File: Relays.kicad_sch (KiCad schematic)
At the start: 28 parts, among them U6 ULN2003

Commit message: Version 1.1
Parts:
- removed IJ1, IJ2, IJ3, IJ4, NCI1, NCI2, NCI3, NCR1, NCR2, NCR3, RJ1, RJ2, RJ3, RJ4: TestPoint, TestPoint:TestPoint_Pad_D1.0mm, symbol Connector:TestPoint
- renumbered R14 to R17, R13 to R18
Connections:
- net RL2: now also U6.6 (I6)
- net RL3: now also U6.4 (I4)
- net RL4: now also U6.2 (I2)
- net at U6.15 (O2): now also RL1.A2, U6.16 (O1)
- net at U6.13 (O4): now also RL2.A2, U6.14 (O3)
- net at RL3.A2, U6.12 (O5): now also U6.11 (O6)

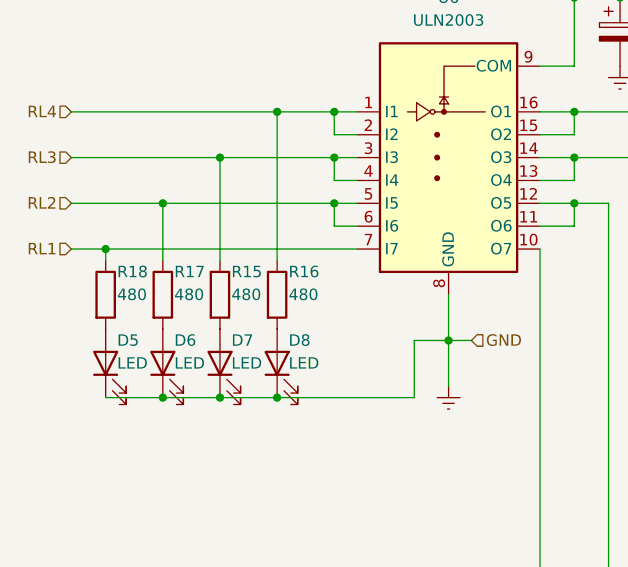
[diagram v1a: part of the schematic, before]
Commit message: Version 1.2 Updates.
Added support for 3 digital switches via ADC.  Added MOV+Fuse protection
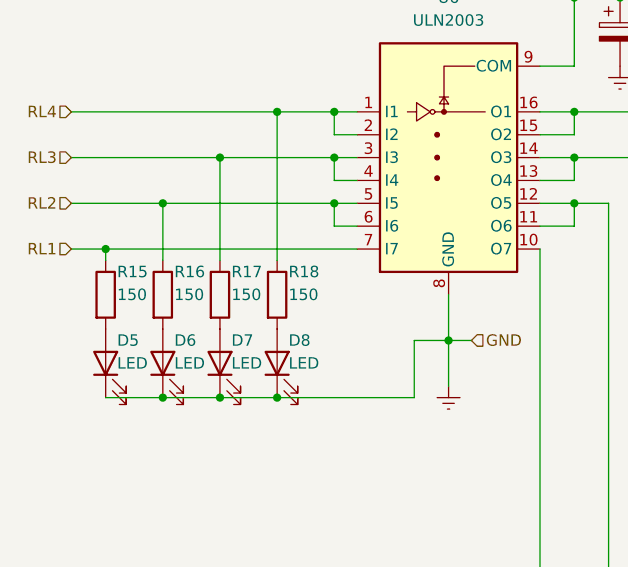
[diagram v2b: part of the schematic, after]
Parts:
- R15: renamed from R18; value 480 -> 150
- R16: renamed from R17; value 480 -> 150
- R17: renamed from R15; value 480 -> 150
- R18: renamed from R16; value 480 -> 150
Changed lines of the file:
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@@
   (symbol (lib_id "Device:R") (at 41.91 107.95 0) (unit 1)
     (in_bom yes) (on_board yes) (dnp no)
-    (property "Reference" "R17" (at 43.18 105.41 0)
-      (effects (font (size 1.27 1.27)) (justify left))
-    )
-    (property "Value" "480" (at 43.18 107.95 0)
+    (property "Reference" "R16" (at 43.18 105.41 0)
+      (effects (font (size 1.27 1.27)) (justify left))
+    )
+    (property "Value" "150" (at 43.18 107.95 0)
       (effects (font (size 1.27 1.27)) (justify left))
     )
@@
       (project "WemosD1Mini-8266"
         (path "/84e8e68d-ec51-4c17-a8b1-603b22d1189f/cc373d62-289d-47e3-a37d-3fec368b320a"
-          (reference "R17") (unit 1)
+          (reference "R16") (unit 1)
         )
       )
@@
   (symbol (lib_id "Device:R") (at 35.56 107.95 0) (unit 1)
     (in_bom yes) (on_board yes) (dnp no)
-    (property "Reference" "R18" (at 36.83 105.41 0)
-      (effects (font (size 1.27 1.27)) (justify left))
-    )
-    (property "Value" "480" (at 36.83 107.95 0)
+    (property "Reference" "R15" (at 36.83 105.41 0)
+      (effects (font (size 1.27 1.27)) (justify left))
+    )
+    (property "Value" "150" (at 36.83 107.95 0)
       (effects (font (size 1.27 1.27)) (justify left))
     )
@@
       (project "WemosD1Mini-8266"
         (path "/84e8e68d-ec51-4c17-a8b1-603b22d1189f/cc373d62-289d-47e3-a37d-3fec368b320a"
-          (reference "R18") (unit 1)
+          (reference "R15") (unit 1)
         )
       )
@@
   (symbol (lib_id "Device:R") (at 48.26 107.95 0) (unit 1)
     (in_bom yes) (on_board yes) (dnp no)
-    (property "Reference" "R15" (at 49.53 105.41 0)
-      (effects (font (size 1.27 1.27)) (justify left))
-    )
-    (property "Value" "480" (at 49.53 107.95 0)
+    (property "Reference" "R17" (at 49.53 105.41 0)
+      (effects (font (size 1.27 1.27)) (justify left))
+    )
+    (property "Value" "150" (at 49.53 107.95 0)
       (effects (font (size 1.27 1.27)) (justify left))
     )
@@
       (project "WemosD1Mini-8266"
         (path "/84e8e68d-ec51-4c17-a8b1-603b22d1189f/cc373d62-289d-47e3-a37d-3fec368b320a"
-          (reference "R15") (unit 1)
+          (reference "R17") (unit 1)
         )
       )
@@
   (symbol (lib_id "Device:R") (at 54.61 107.95 0) (unit 1)
     (in_bom yes) (on_board yes) (dnp no)
-    (property "Reference" "R16" (at 55.88 105.41 0)
-      (effects (font (size 1.27 1.27)) (justify left))
-    )
-    (property "Value" "480" (at 55.88 107.95 0)
+    (property "Reference" "R18" (at 55.88 105.41 0)
+      (effects (font (size 1.27 1.27)) (justify left))
+    )
+    (property "Value" "150" (at 55.88 107.95 0)
       (effects (font (size 1.27 1.27)) (justify left))
     )
@@
       (project "WemosD1Mini-8266"
         (path "/84e8e68d-ec51-4c17-a8b1-603b22d1189f/cc373d62-289d-47e3-a37d-3fec368b320a"
-          (reference "R16") (unit 1)
-        )
-      )
+          (reference "R18") (unit 1)
+        )
+      )
